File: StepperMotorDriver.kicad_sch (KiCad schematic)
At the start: 26 parts, among them Q10 ULN2003D1013TR, Q11 ULN2003ADR

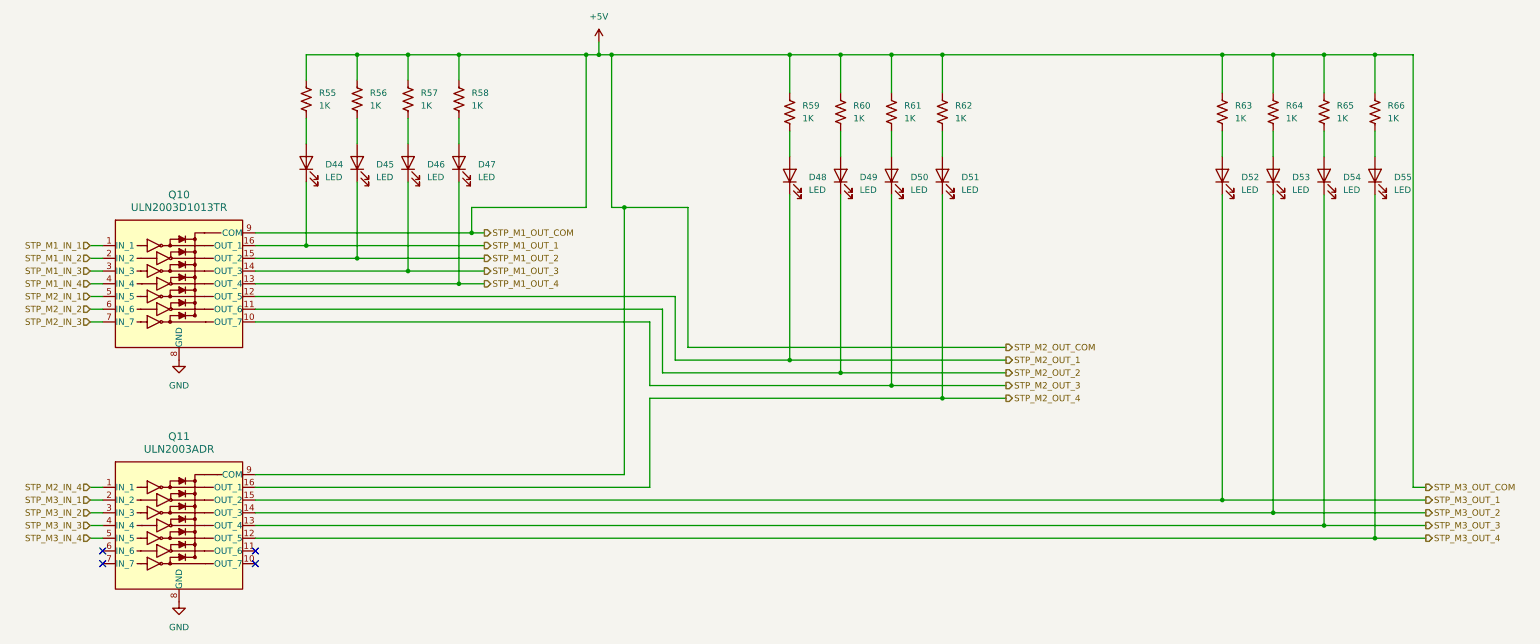
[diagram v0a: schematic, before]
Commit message: PCB 90% & Corrections to diagram in the ADC section were done
Te resistors to secure a low logical level were placed, also the routing of the PCB is at the 90%
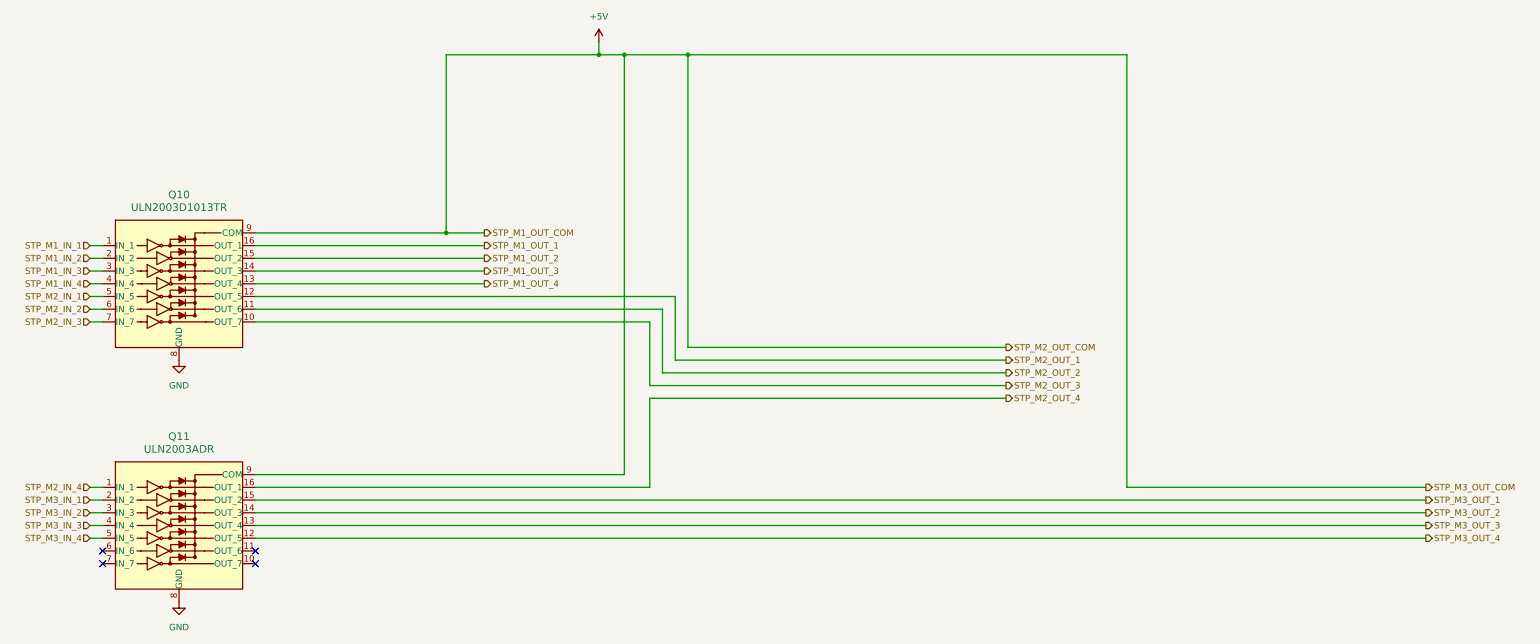
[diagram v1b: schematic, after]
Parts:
- removed D44, D45, D46, D47, D48, D49, D50, D51, D52, D53, D54, D55: LED, LED_THT:LED_D3.0mm, symbol Device:LED
- removed R55, R56, R57, R58, R59, R60, R61, R62, R63, R64, R65, R66: 1K, Resistor_THT:R_Axial_DIN0204_L3.6mm_D1.6mm_P5.08mm_Horizontal, symbol Device:R_US
